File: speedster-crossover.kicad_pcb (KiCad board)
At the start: 2 copper layers, 184 x 125 mm, 20 parts, among them X1 HP INPUT, X2 LP INPUT

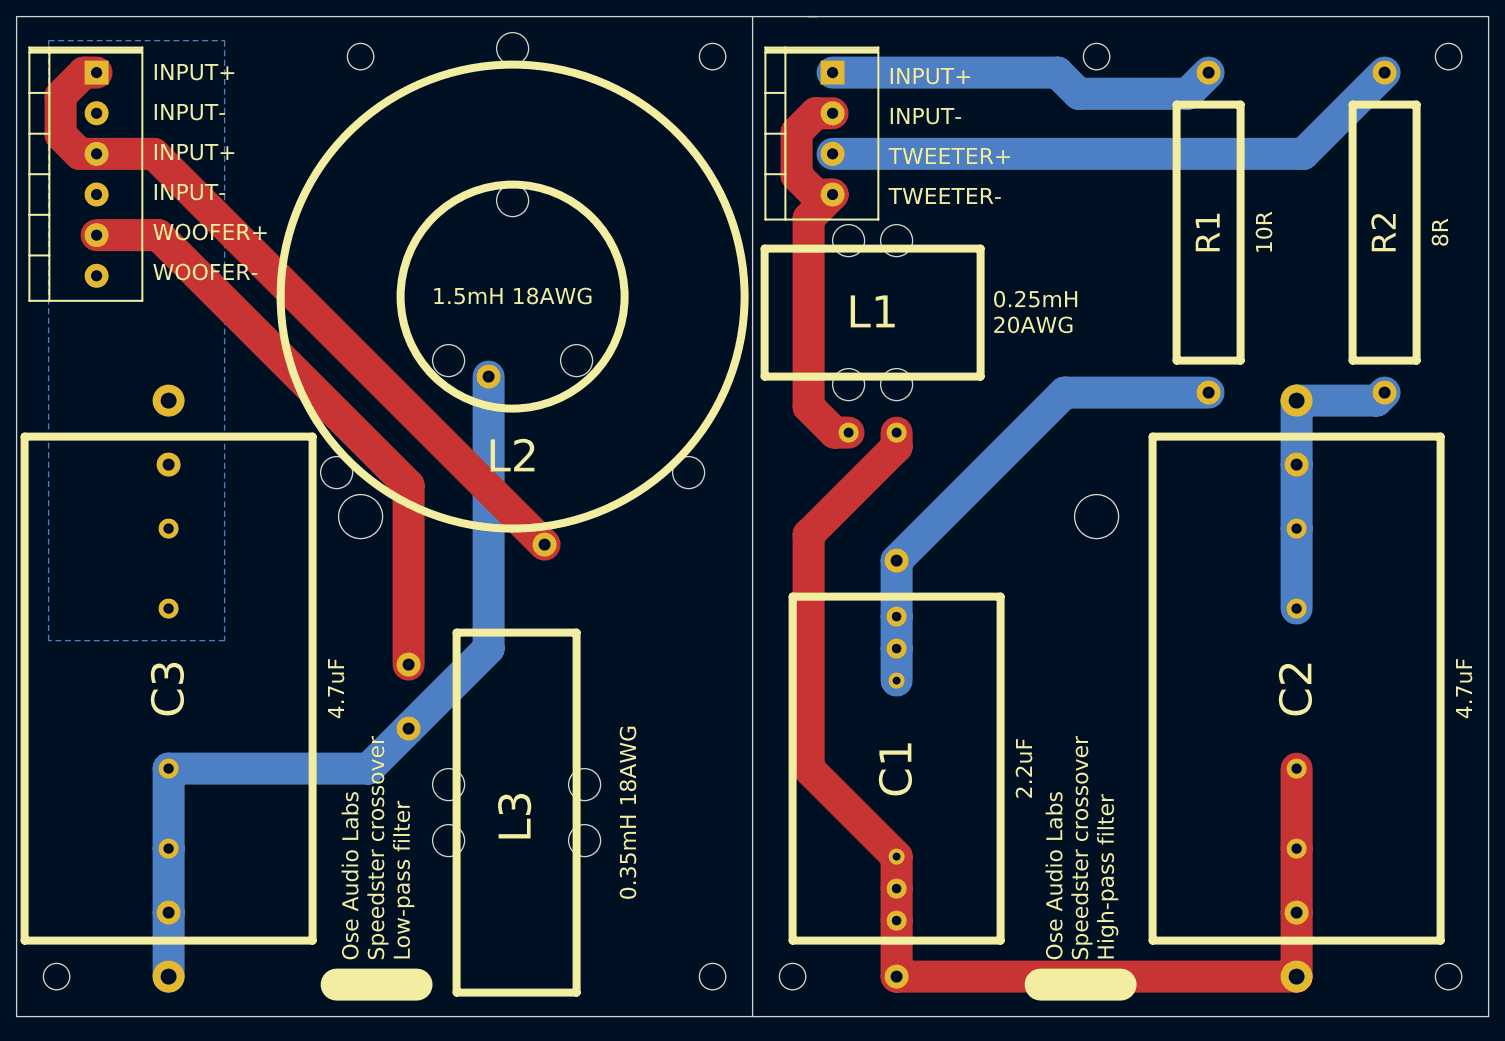
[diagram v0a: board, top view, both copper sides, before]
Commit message: Updates to layout
- smaller L3 footprint
- tighter C1 lead spacing
- alternative quick-disconnect pins for X1/2
  (http://www.mcmaster.com/#7956k5/=10cwxu4)
- plated mounting holes
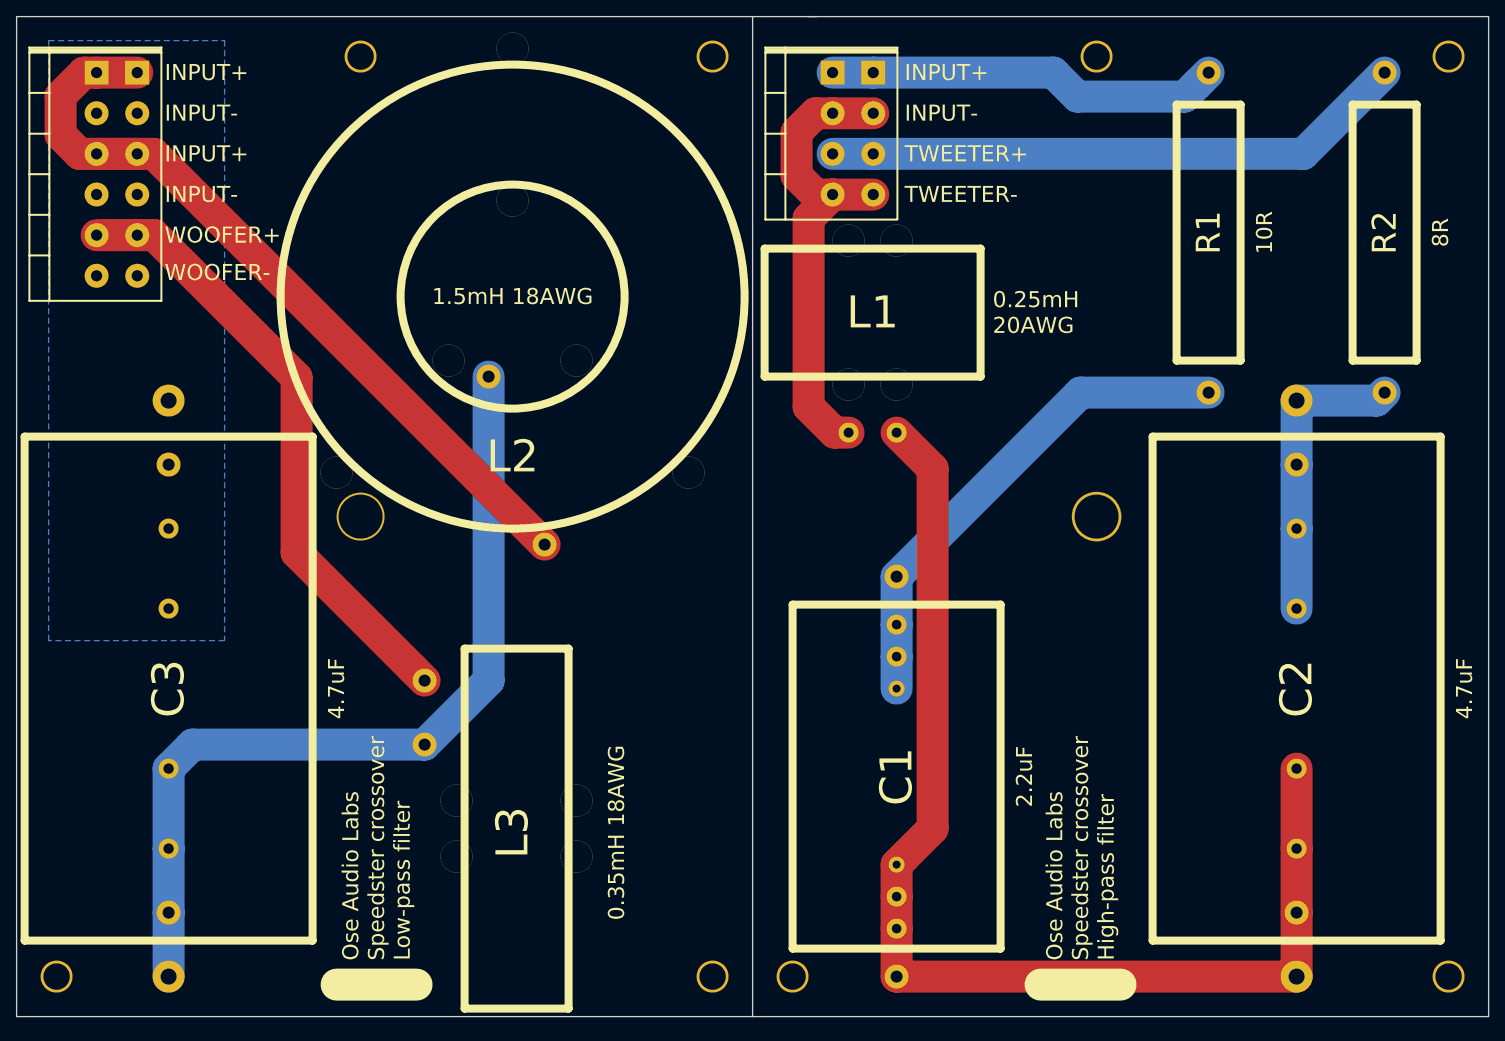
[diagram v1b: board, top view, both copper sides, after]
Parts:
- moved L3 2.24 mm to (100.0, 108.0)
- moved C1 1.00 mm to (154.0, 124.0)
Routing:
- net HPINPUT-: track 50.5 -> 60.6 mm
- net LPINPUT+: track 92.3 -> 102.4 mm
- net Net-(C1-Pad1): track 153.1 -> 147.7 mm
- net WOOFER+: track 74.4 -> 76.9 mm
- net Net-(C3-Pad1): track 106.2 -> 108.6 mm

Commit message: Fine tune some lead spacing, back silkscreen logo
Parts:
- added G***: LOGO, OAL_logo, F.Cu at (190.0, 54.0)
- added G***: LOGO, OAL_logo, F.Cu at (90.0, 54.0)
- moved R1 1.00 mm to (193.0, 55.0)
- moved R2 1.00 mm to (215.0, 55.0)
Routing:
- net Net-(C1-Pad1): track 147.7 -> 162.1 mm
- net Net-(C2-Pad2): track 37.4 -> 38.2 mm

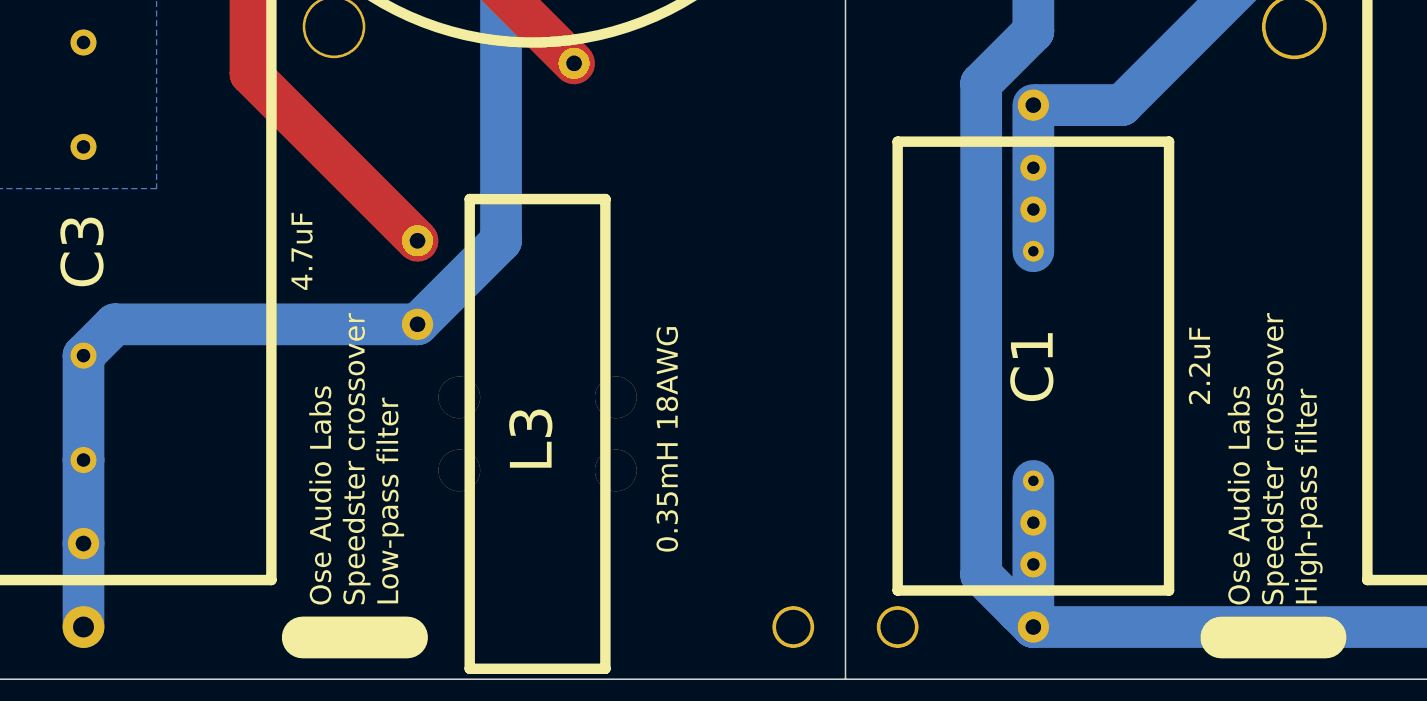
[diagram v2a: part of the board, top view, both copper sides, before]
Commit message: add license, update logos
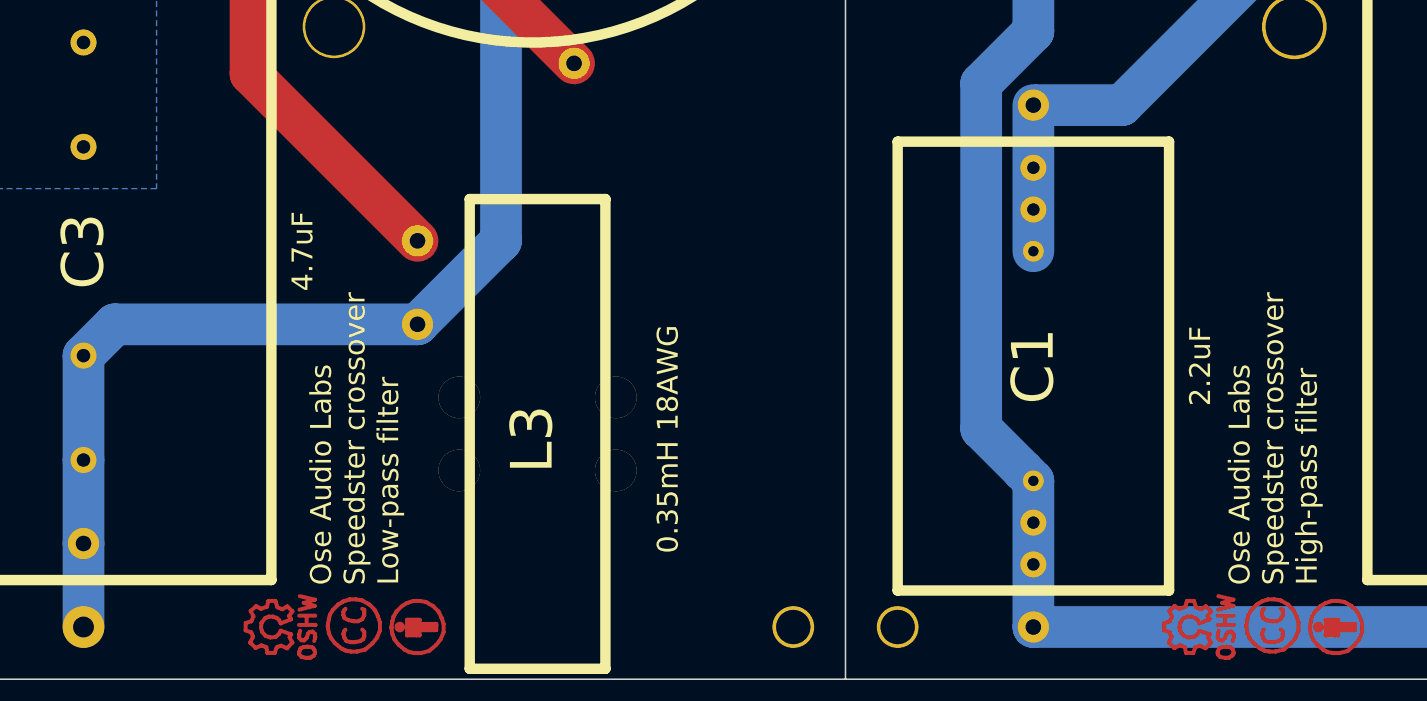
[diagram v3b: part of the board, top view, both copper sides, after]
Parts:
- removed the G*** at (190.0, 54.0)
- removed the G*** at (90.0, 54.0)
- added G***: LOGO, OAL_logo, F.Cu at (112.0, 54.0)
- added G***: LOGO, OAL_logo, F.Cu at (204.0, 54.0)
- added REF**: Symbol_OSHW-Logo_CopperTop, Symbols:Symbol_OSHW-Logo_CopperTop, F.Cu at (169.0, 149.0)
- added REF**: Symbol_CC-Attribution_CopperTop_Small, Symbols:Symbol_CC-Attribution_CopperTop_Small, F.Cu at (183.0, 149.0)
- added REF**: Symbol_CreativeCommons_CopperTop_Type2_Small, Symbols:Symbol_CreativeCommons_CopperTop_Type2_Small, F.Cu at (177.0, 149.0)
- added REF**: Symbol_CreativeCommons_CopperTop_Type2_Small, Symbols:Symbol_CreativeCommons_CopperTop_Type2_Small, F.Cu at (89.0, 149.0)
- added REF**: Symbol_OSHW-Logo_CopperTop, Symbols:Symbol_OSHW-Logo_CopperTop, F.Cu at (81.0, 149.0)
- added REF**: Symbol_CC-Attribution_CopperTop_Small, Symbols:Symbol_CC-Attribution_CopperTop_Small, F.Cu at (95.0, 149.0)
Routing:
- net Net-(C1-Pad1): track 162.1 -> 148.1 mm
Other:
- board text added: "(C) Greg Ose 2015 http://github.com/gregose/speedster-crossover"

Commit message: final tweaks before fab
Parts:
- moved ? 1.00 mm to (223.0, 150.0)
- moved L2 1.00 mm to (106.0, 63.0)
- moved REF** 1.00 mm to (131.0, 150.0)
- moved REF** 1.00 mm to (141.0, 150.0)
- moved REF** 1.00 mm to (49.0, 150.0)
- moved REF** 1.00 mm to (169.0, 150.0)
- moved REF** 1.00 mm to (183.0, 150.0)
- moved REF** 1.00 mm to (177.0, 150.0)
- moved REF** 1.00 mm to (89.0, 150.0)
- moved REF** 1.00 mm to (81.0, 150.0)
- moved REF** 1.00 mm to (95.0, 150.0)
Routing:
- net LPINPUT+: track 102.4 -> 97.0 mm
- net Net-(C3-Pad1): track 108.6 -> 110.0 mm
- net Net-(C1-Pad1): track 148.1 -> 149.0 mm
- net HPINPUT+: track 49.5 -> 50.3 mm
- net Net-(C1-Pad2): track 62.9 -> 63.4 mm
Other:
- board size 184 x 125 mm -> 184 x 126 mm
- net class Default: trace_width 4 -> 5
- board text added: "(C) Greg Ose 2015 http://github.com/gregose/speedster-crossover Circuit designed by Paul Carmody"
- board text added: "Ose Audio Labs Speedster crossover (Rev. A) High-pass filter"
- board text added: "Ose Audio Labs Speedster crossover (Rev. A) Low-pass filter"
- board text removed: "(C) Greg Ose 2015 http://github.com/gregose/speedster-crossover"
- board text removed: "Ose Audio Labs Speedster crossover High-pass filter"
- board text removed: "Ose Audio Labs Speedster crossover Low-pass filter"
